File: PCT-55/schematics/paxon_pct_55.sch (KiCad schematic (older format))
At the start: 606 parts, among them IC1 TA7607AP, IC2 UPC1382C, IC201 HA11431, IC202 TA7676AP, IC301 HA11423, IC502 _, IC901 TC4052BP, IC902 TC4052BP, IC950 HD7407, J401 CONN_01x05, J403 CONN_01x04, J404 CONN_01x07, J503 CONN_01x04, J503-1 CONN_01x04, J505 CONN_01x02, J903 CONN_01x02, J913 CONN_01x05, J918 CONN_01x02, J919 CONN_01x04, J920 CONN_01x08, J921 CONN_01x06, J927 CONN_01x03, K1 CONN_01x03, P402 CONN_01x03, P504 CONN_01x09, P801 CONN_01x03, P802 CONN_01x03, P901 CONN_01x09, P902 CONN_01x06, P903 CONN_01x02, P911 CONN_01x05, P912 CONN_01x02, P913 CONN_01x05, P914 CONN_01x04, P917 CONN_01x02, P918 CONN_01x02, P919 CONN_01x04, P927 CONN_01x03, Q1 C388A_NPN_BCE, Q2 C2458_NPN_BCE, Q202 A854_PNP_BCE, Q203 A1015_PNP_BCE, Q204 A1015_PNP_BCE, Q301 C2073_NPN_BCE, Q302 C2073_NPN_BCE, Q303 A1015_PNP_BCE, Q304 C1815_NPN_BCE, Q351 C2610_NPN_BCE, Q352 D1425_NPN_BCE, Q451 D758_NPN_BCE, Q452 D758_NPN_BCE, Q453 D758_NPN_BCE, Q454 C1815_NPN_BCE, Q455 C1815_NPN_BCE, Q456 C1815_NPN_BCE, Q501 A1015_PNP_BCE, Q502 C1815_NPN_BCE, Q503 C2236_NPN_CBE, Q504 2SC2122A_NPN_BCE, Q505 D1052A_NPN_BCE, Q551 A733_PNP_BCE, Q801 C1815_NPN_BCE, Q802 A950_PNP_BCE, Q803 C2120_NPN_BCE, Q901 A952_PNP_BCE, Q902 C1815_NPN_BCE, Q903 A733_PNP_BCE, Q905 ???, Q906 ???, Q950 C1815_NPN_BCE, Q951 A950_PNP_BCE, Q952 C2120_NPN_BCE, Q953 C1815_NPN_BCE, Q954 C1815_NPN_BCE, Q955 C1815_NPN_BCE, SW1 CH1, SW10 MSX, SW2 CH2, SW3 CH3, SW4 CH4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

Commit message: Add files via upload
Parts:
- added Audiojackswitch1: SW_DPDT_x2, symbol Switch:SW_DPDT_x2
- added C32: 10uf/25v, symbol Device:CP1_Small
- added CF1: T4.5MB, symbol RF_Filter:CF_filter
- added CF2: SFE 4.5MB, symbol RF_Filter:CF_filter
- added CF3: CDA 4.5MB, symbol RF_Filter:CF_filter
- added FL1: F1021S, symbol RF_Amplifier:F1021S
- added J1: Audiojack with switch, symbol Connector:AudioJack2
- added LS1: Speaker, symbol Device:Speaker
- added R15: 1K8, symbol agg-kicad:R
- added R38: 560R, symbol agg-kicad:R
- C10: value ??? -> <5pF
- C12, C27: value ??? -> 4.7uf/50v
- C14: value ??? -> 100uf/16v
- C15, C16: value ??? -> 0.47uf/50v
- C21: value 10uf/25v -> 47uf/16v
- C23: value ??? -> 10uf/25v
- C26: value ??? -> 1uf/50v
- IC502: value _ -> NEC uPC574
- L10: value ??? -> 80uH
- L5: value ??? -> 20uH
- R36: value ??? -> 1K
- renumbered C21 to C40, C19 to C41
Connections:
- net labels added: IF_BOX_pin_10, IF_BOX_pin_11, IF_BOX_pin_2
- net labels removed: IF-BOX-pin_10, IF-BOX-pin_11, TUNER_BOX_pin_1, TUNER_BOX_pin_10, TUNER_BOX_pin_11, TUNER_BOX_pin_2, TUNER_BOX_pin_3, TUNER_BOX_pin_4, TUNER_BOX_pin_5, TUNER_BOX_pin_6, TUNER_BOX_pin_7, TUNER_BOX_pin_8, TUNER_BOX_pin_9
- wire segments 2429 -> 2446
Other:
- note added: "(CCC) wires to J503\nin AV+ParallelPort input PCB"
- note added: "(CCC) wires to J503\nin main pcb"
- note added: "(FFF) wires to P504\nin main PCB"
- note added: "(FFF) wires to P901\nin front PCB"
- note added: "(HHH) wires,\nfrom P301 in main PCB"
- note added: "(JJJ) wires to J903\nin 4CEC PCB"
- note added: "(JJJ) wires\nto P903 in front PCB\n (where channel/msx/av switches are)"
- note added: "(KKK) wires,\nfrom 4CEC PCB"
- note added: "(LLL) wires to J913\nin AV+ParallelPort input PCB"
- note added: "(LLL) wires to P913\nin 4CEB PCB"
- note added: "(MMM) wires to J918\nin AV+ParallelPort input PCB"
- note added: "(MMM) wires to P918\nin 4CEC"
- note added: "(OOO) wires to P919\nin 4CEC PCB"
- note added: "(OOO) wires\nto AV+ParallelPort input PCB"
- note added: "(RRR) wires to CONN-10\nin MSX PCB"
- note added: "(SSS) wires to \nmono speaker\nand mono headphone socket"
- note added: "(UUU) wires to CONN-6\nin MSX PCB"
- note added: "(WWW) wires to CONN-1\nin MSX PCB"
- note added: "(ZZZ) wires to J927\nin AV+ParallelPort input PCB"
- note added: "(ZZZ) wires to P927\nin main PCB"
- note added: "+5V , white wire\n"
- note added: "-15V\n"
- note added: "1"
- note added: "1 = white wire\n"
- note added: "1. = white wire"
- note added: "1. = white wire\n"
- note added: "15V"
- note added: "2"
- note added: "3"
- note added: "C40 and C41 are under pcb \nwithout any Cxx marks on pcb"
- note added: "FL1 pinout numbers not known, so not correct!\nJust illustrating from \nunder the pcb the pin locations"
- note added: "G 1. white wire\nR\nB"
- note added: "J505 goes to P912 in 4CEB PCB"
- note added: "L6"
- note added: "P801 pins:"
- note added: "Separate black thick ground wires towards:\n-tube ground\n-tuner box metal\n-AV+ParallelPort input PCB\n\nThere is also thick black wire from \ndigital RGB pcb to tuner box metal"
- note added: "from\nMSX PCB"
- note added: "mono 3.5mm audiojack:\n-when headphones connected, connect ground to head phones ground\n-when no headphones connected, connect ground to speaker"
- note added: "to AV+ParallelPort input PCB,\nDigital RGB to analog conversion applitude?"
- note added: "to Volume pot\n(AAA) wires"
- note removed: "(CCC) wires,\nto Digital RGB input pcb ->J503"
- note removed: "(CCC) wires,\nto main pcb, J503\nwhite=5V"
- note removed: "(FFF) wires"
- note removed: "(FFF) wires\nto main PCB"
- note removed: "(HHH) wires,\nfrom main PCB"
- note removed: "(JJJ) marked to wires\nto front PCB\n (where channel/msx/av switches are)\n-> P903 connector"
- note removed: "(JJJ) wires\nto 5v enable \nin main pcb\n( J903 )\n"
- note removed: "(KKK) wires,\nfrom main PCB"
- note removed: "(LLL) wires"
- note removed: "(MMM) marked to wires\nto digital RGB input PCB:\n-> J918 connector"
- note removed: "(MMM) wires"
- note removed: "(OOO) wires"
- note removed: "(RRR) wires,\nto MSX pcb, CONN-10"
- note removed: "(WWW) wires,\nto MSX pcb,CONN-1"
- note removed: "(ZZZ) wires"
- note removed: "(ZZZ) wires,\nto main PCB, P927"
- note removed: "+15V ?"
- note removed: "-15V ?\n"
- note removed: "A"
- note removed: "B"
- note removed: "CF1\nT4.5B"
- note removed: "CF2 \nSF5\n4.5MB"
- note removed: "CF3\nCDA\n4.5MB"
- note removed: "G = white wire\nR\nB"
- note removed: "J505 goes to P912"
- note removed: "L9"
- note removed: "MSX"
- note removed: "Separate black thick ground wires towards:\n-tube ground\n-tuner box metal\n-digital RGB board\n\nThere is also thick black wire from \ndigital RGB pcb to tuner box metal"
- note removed: "switch 5V power off from main pcb"
- note removed: "to Digital RGB PCB,\nRGB input conversion applitude?"
- note removed: "to MSX PCB, CONN-6\n(UUU) marked to wires"
- note removed: "to Volume pot"
- note removed: "to front PCB"
- note removed: "white wire"
- note removed: "white wire is pin 1\n"
- note removed: "white\n"

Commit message: Add files via upload
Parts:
- renumbered VR1 to VR251
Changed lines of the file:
@@
 	17960 13840 19360 13840
 $Comp
-L Device:R_POT VR1
+L Device:R_POT VR251
 U 1 1 B6B875F4
 P 18320 14150
-F 0 "VR1" H 18250 14180 50  0000 R CNN
+F 0 "VR251" H 18250 14180 50  0000 R CNN
 F 1 "???" H 18220 14100 50  0000 R CNN
 F 2 "" H 18320 14150 50  0001 C CNN

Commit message: Add files via upload
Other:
- note added: "IF BOX PCB"
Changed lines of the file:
@@
 Text Notes 10480 5260 0    51   ~ 0
 P801 pins:
+Wire Notes Line
+	23870 340  29870 340
+Wire Notes Line
+	29870 340  29870 6320
+Wire Notes Line
+	29870 6320 23860 6320
+Wire Notes Line
+	23860 6320 23860 340
+Text Notes 23930 590  0    157  ~ 31
+IF BOX PCB
 $EndSCHEMATC

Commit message: Add files via upload
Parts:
- added J915: CONN_01x11, symbol agg-kicad:CONN_01x11
- added J924: Centronics 14-pin, symbol Connector_Generic:Conn_02x07_Top_Bottom
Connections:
- wire segments 2446 -> 2488
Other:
- note added: "(XXX) wires to\nCONN-9 in MSX PCB"
- note added: "AV input + ParallelPort PCB:\n-rca video + audio input\n-RGB digital input\n-MSX parallel port"
- note removed: "DIGITAL RGB input pcb:\n(also contains rca input for video/audio)"
- moved on the sheet: C950, C956, C957, C958, C959, L950, Q954, Q955, R970, R971, R972, R973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

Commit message: initial msx pcb, just components, no wirings
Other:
- note added: "1. =white wire\n"
- note removed: "white wire\n"
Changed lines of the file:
@@
 $Descr A2 23386 16535
 encoding utf-8
-Sheet 1 1
+Sheet 1 2
 Title ""
 Date ""
@@
 (ZZZ) wires to P927\nin main PCB
 Text Notes 5740 1900 0    50   ~ 0
-white wire\n
+1. =white wire\n
 $Comp
 L agg-kicad:CONN_01x03 J927
@@
 Wire Wire Line
 	3310 3570 3490 3570
+$Sheet
+S 24750 7580 3540 2220
+U 65EF74FD
+F0 "MSX pacb" 51
+F1 "msx_pcb.sch" 51
+$EndSheet
 $EndSCHEMATC

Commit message: Add files via upload
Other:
- note added: "(CCC) wires to J503\nin AV input+PrinterPort PCB"
- note added: "(LLL) wires to J913\nin AV input+PrinterPort PCB"
- note added: "(MMM) wires to J918\nin AV input+PrinterPort PCB"
- note added: "(OOO) wires\nto AV input+PrinterPort PCB"
- note added: "(ZZZ) wires to J927\nin AV input+PrinterPort PCB"
- note added: "AV input + Printer Port PCB:\n-rca video + audio input\n-RGB digital input\n-MSX printer port"
- note added: "Separate black thick ground wires towards:\n-tube ground\n-tuner box metal\n-AV input+PrinterPort PCB\n\nThere is also thick black wire from \ndigital RGB pcb to tuner box metal"
- note added: "to AV input+Printer Port PCB,\nDigital RGB to analog conversion applitude?"
- note removed: "(CCC) wires to J503\nin AV+ParallelPort input PCB"
- note removed: "(LLL) wires to J913\nin AV+ParallelPort input PCB"
- note removed: "(MMM) wires to J918\nin AV+ParallelPort input PCB"
- note removed: "(OOO) wires\nto AV+ParallelPort input PCB"
- note removed: "(ZZZ) wires to J927\nin AV+ParallelPort input PCB"
- note removed: "AV input + ParallelPort PCB:\n-rca video + audio input\n-RGB digital input\n-MSX parallel port"
- note removed: "Separate black thick ground wires towards:\n-tube ground\n-tuner box metal\n-AV+ParallelPort input PCB\n\nThere is also thick black wire from \ndigital RGB pcb to tuner box metal"
- note removed: "to AV+ParallelPort input PCB,\nDigital RGB to analog conversion applitude?"
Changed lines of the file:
@@
 (JJJ) wires\nto P903 in front PCB\n (where channel/msx/av switches are)
 Text Notes 9790 8390 0    50   ~ 0
-(MMM) wires to J918\nin AV+ParallelPort input PCB
+(MMM) wires to J918\nin AV input+PrinterPort PCB
 Wire Wire Line
 	9630 8310 9630 8680
@@
 	-340 4780 -340 170
 Text Notes 130  380  0    157  ~ 31
-AV input + ParallelPort PCB:\n-rca video + audio input\n-RGB digital input\n-MSX parallel port
+AV input + Printer Port PCB:\n-rca video + audio input\n-RGB digital input\n-MSX printer port
 $Comp
 L agg-kicad:CONN_01x06 P902
@@
 $EndComp
 Text Notes 12970 5510 0    50   ~ 0
-(ZZZ) wires to J927\nin AV+ParallelPort input PCB
+(ZZZ) wires to J927\nin AV input+PrinterPort PCB
 Text Notes 13580 5700 0    50   ~ 0
 1. = white wire\n
@@
 IC202_R_DATA_IN
 Text Notes 9710 7220 0    50   ~ 0
-(OOO) wires\nto AV+ParallelPort input PCB
+(OOO) wires\nto AV input+PrinterPort PCB
 Text Notes 11800 8280 0    50   ~ 0
 G  1. white wire\nR\nB
@@
 	16980 15500 16980 15620
 Text Notes 17020 14850 0    50   ~ 0
-to AV+ParallelPort input PCB,\nDigital RGB to analog conversion applitude?
+to AV input+Printer Port PCB,\nDigital RGB to analog conversion applitude?
 $Comp
 L power:GND #PWR0229
@@
 	8310 15060 8370 15060
 Text Notes 15430 11590 0    59   ~ 0
-(LLL) wires to J913\nin AV+ParallelPort input PCB
+(LLL) wires to J913\nin AV input+PrinterPort PCB
 Text Notes 20120 10830 0    50   ~ 0
 L207 coil color code:\nBlack-Black-Brown-Gold
@@
 SelectB
 Text Notes 9550 6120 0    50   ~ 0
-(CCC) wires to J503\nin AV+ParallelPort input PCB
+(CCC) wires to J503\nin AV input+PrinterPort PCB
 Text Notes 13790 1810 0    50   ~ 0
 <-blue wire->
@@
 	19100 2820 19190 2820
 Text Notes 20890 1170 0    50   ~ 0
-Separate black thick ground wires towards:\n-tube ground\n-tuner box metal\n-AV+ParallelPort input PCB\n\nThere is also thick black wire from \ndigital RGB pcb to tuner box metal
+Separate black thick ground wires towards:\n-tube ground\n-tuner box metal\n-AV input+PrinterPort PCB\n\nThere is also thick black wire from \ndigital RGB pcb to tuner box metal
 Text Notes 20340 730  0    118  ~ 24
 NOTE!

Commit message: shuold be now final
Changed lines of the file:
@@
 encoding utf-8
 Sheet 1 2
-Title ""
+Title "Paxon PCT-55 schematics by Popolon_"
 Date ""
 Rev ""
 Comp ""
-Comment1 ""
+Comment1 "RF box schematics is not drawn"
 Comment2 ""
 Comment3 ""
@@
 C40 and C41 are under pcb \nwithout any Cxx marks on pcb
 $Comp
-L power:GND #PWR?
+L power:GND #PWR0281
 U 1 1 66984339
 P 28380 4740
-F 0 "#PWR?" H 28380 4490 50  0001 C CNN
+F 0 "#PWR0281" H 28380 4490 50  0001 C CNN
 F 1 "GND" H 28610 4690 50  0000 R CNN
 F 2 "" H 28380 4740 50  0001 C CNN
@@
 $EndComp
 $Comp
-L power:GND #PWR?
+L power:GND #PWR0282
 U 1 1 68458DD5
 P 25440 2290
-F 0 "#PWR?" H 25440 2040 50  0001 C CNN
+F 0 "#PWR0282" H 25440 2040 50  0001 C CNN
 F 1 "GND" H 25370 2230 50  0000 R CNN
 F 2 "" H 25440 2290 50  0001 C CNN
@@
 S 24750 7580 3540 2220
 U 65EF74FD
-F0 "MSX pacb" 51
+F0 "MSX PCB" 51
 F1 "msx_pcb.sch" 51
 $EndSheet

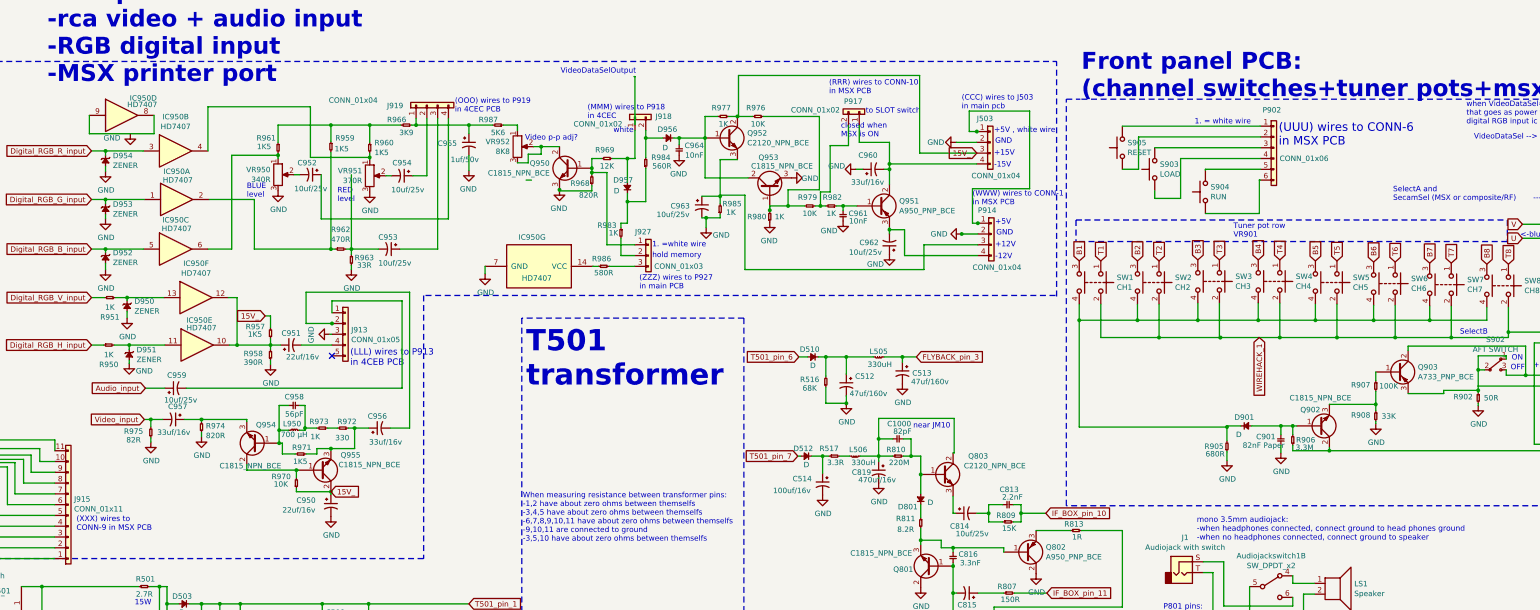
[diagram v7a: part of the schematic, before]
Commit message: added filter caps and relay symbol for MSX pcb
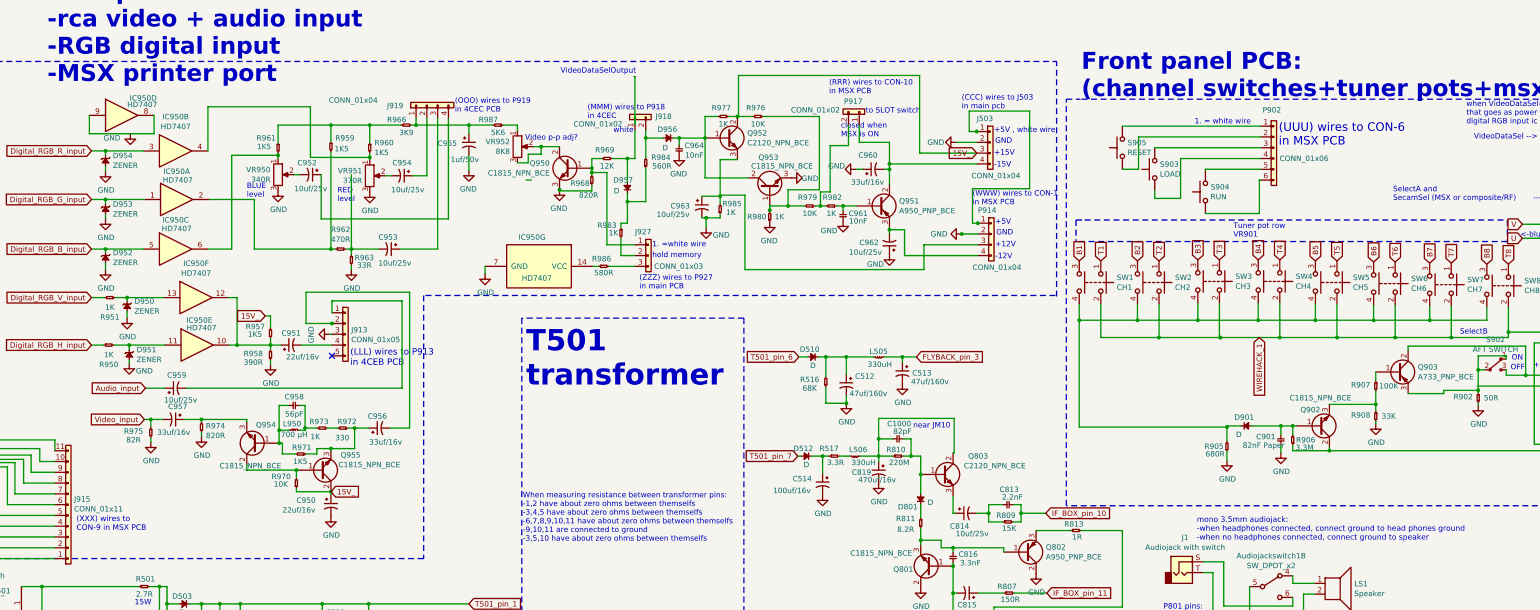
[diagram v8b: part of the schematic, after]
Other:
- note added: "(RRR) wires to CON-10\nin MSX PCB"
- note added: "(UUU) wires to CON-6\nin MSX PCB"
- note added: "(WWW) wires to CON-1\nin MSX PCB"
- note added: "(XXX) wires to\nCON-9 in MSX PCB"
- note removed: "(RRR) wires to CONN-10\nin MSX PCB"
- note removed: "(UUU) wires to CONN-6\nin MSX PCB"
- note removed: "(WWW) wires to CONN-1\nin MSX PCB"
- note removed: "(XXX) wires to\nCONN-9 in MSX PCB"
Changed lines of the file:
@@
 	10250 870  11380 870
 Text Notes 11550 960  0    79   ~ 0
-(UUU) wires to CONN-6\nin MSX PCB
+(UUU) wires to CON-6\nin MSX PCB
 Text Notes 9720 520  0    157  ~ 31
 Front panel PCB:\n(channel switches+tuner pots+msx reset/load/run buttons)
@@
 (MMM) wires to P918\nin 4CEC
 Text Notes 8710 1510 0    50   ~ 0
-(WWW) wires to CONN-1\nin MSX PCB
+(WWW) wires to CON-1\nin MSX PCB
 Text Notes 8610 620  0    50   ~ 0
 (CCC) wires to J503\nin main pcb
 Text Notes 7380 480  0    50   ~ 0
-(RRR) wires to CONN-10\nin MSX PCB
+(RRR) wires to CON-10\nin MSX PCB
 $Comp
 L agg-kicad:CONN_01x09 P901
@@
 $EndComp
 Text Notes 400  4530 0    51   ~ 0
-(XXX) wires to\nCONN-9 in MSX PCB
+(XXX) wires to\nCON-9 in MSX PCB
 $Comp
 L Connector_Generic:Conn_02x07_Top_Bottom J924
